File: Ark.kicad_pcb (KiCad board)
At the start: 2 copper layers, 71.9 x 89.1 mm, 109 parts, among them P1 USB_OTG, P2 USB_OTG, P3 40_Pin_LCD_Out, P4 6_Pin_Touch_In, Q1 MMUN2133LT1G, SW1 SW_PUSH_SMALL_H, SW2 SW_PUSH_SMALL_H, SW3 SW_PUSH_SMALL_H, SW4 SW_PUSH_SMALL_H, SW5 SW_PUSH_SMALL_H, SW6 SW_PUSH_SMALL_H, U1 PAM2306AYPKE, U2 AP7115-25SEG, U3 DDR2_SODIMM_CM_3_Lite, U4 1040310811, U5 FAN5333BSX, U6 TPS61090RSAR, U7 MCP73871, U8 SPDT_switch

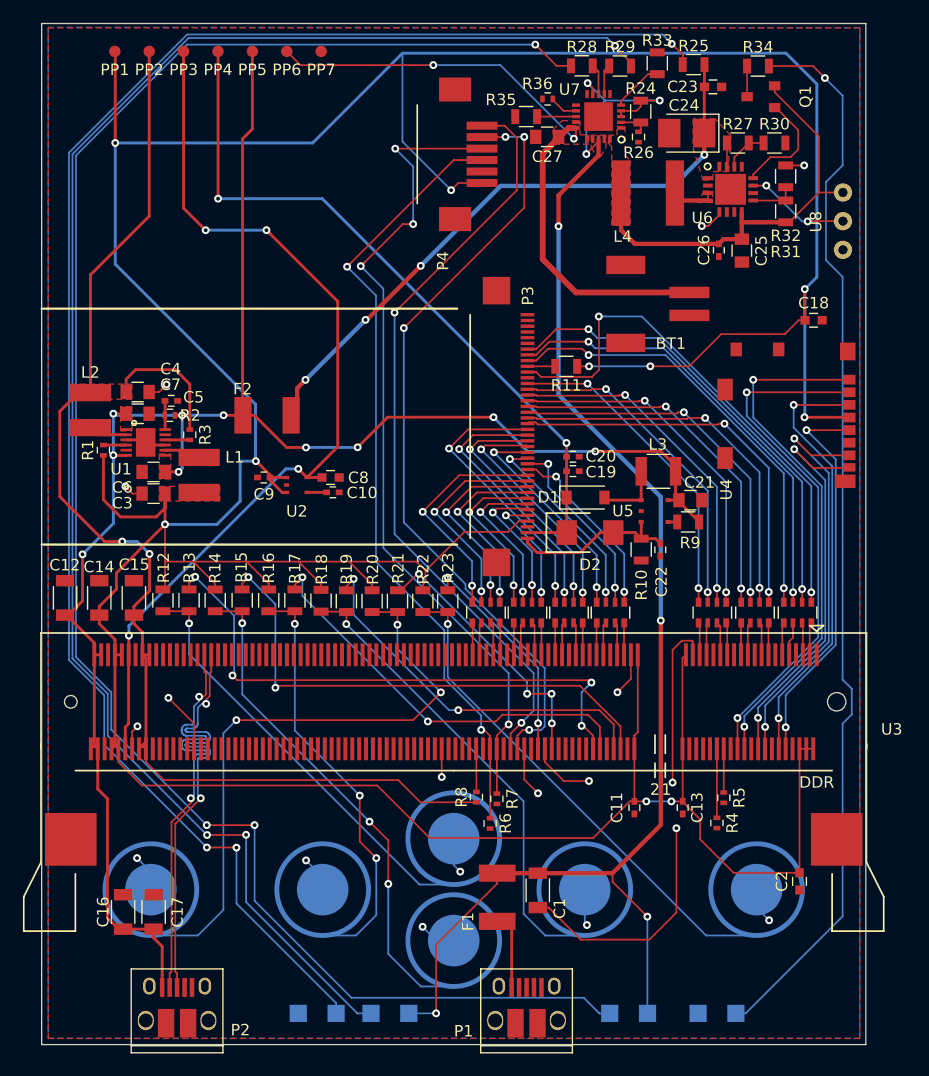
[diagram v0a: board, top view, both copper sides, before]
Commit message: Added grouding vias
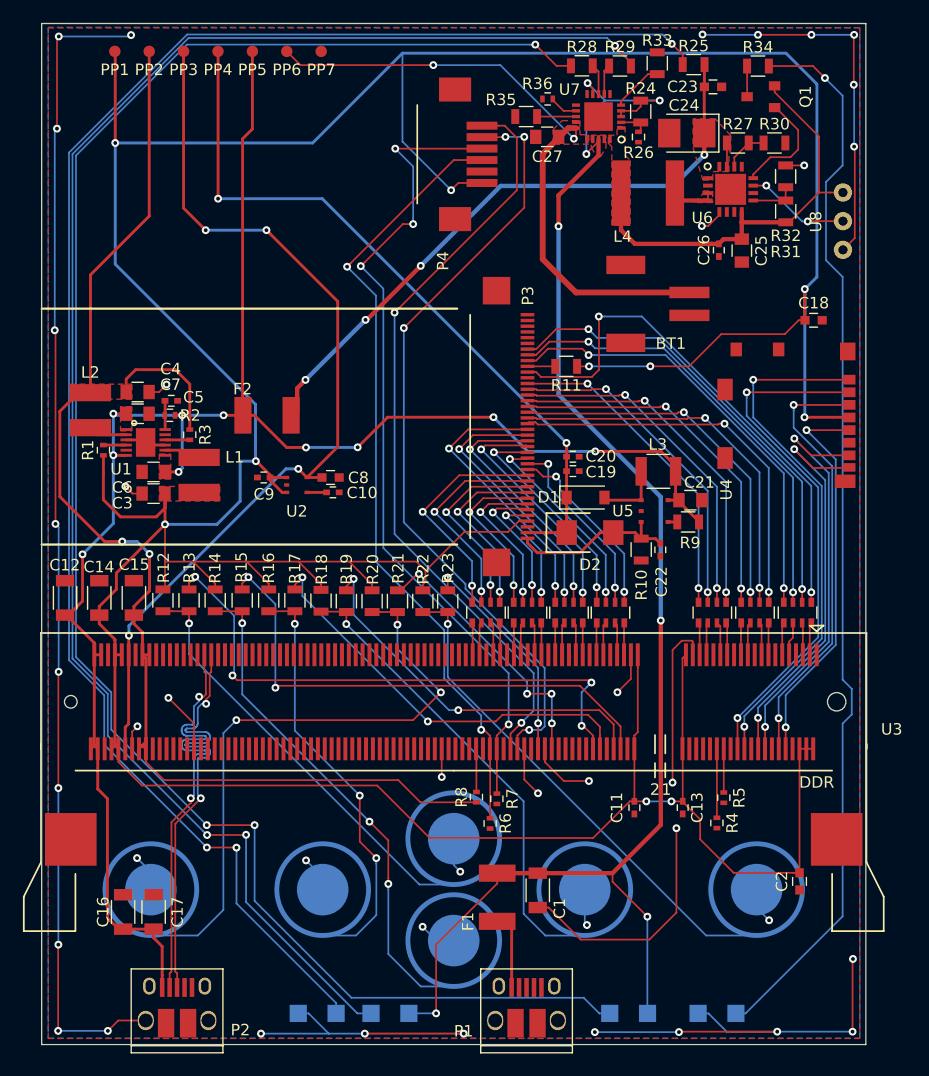
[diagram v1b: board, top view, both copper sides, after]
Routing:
- net GND: track 90.2 -> 290.1 mm, vias 18 -> 42
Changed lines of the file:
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@@
     (thickness 1.6002)
     (drawings 12)
-    (tracks 1414)
+    (tracks 1482)
     (zones 0)
     (modules 109)
@@
   (gr_line (start 103.759 167.0558) (end 175.641 167.0558) (layer Edge.Cuts) (width 0.1))
   (gr_line (start 103.759 78) (end 175.641 78) (layer Edge.Cuts) (width 0.1))
+  (segment (start 105.25252 79.13116) (end 111.43488 79.13116) (width 0.1524) (layer B.Cu) (net 1))
+  (segment (start 111.43488 79.13116) (end 111.5568 79.00924) (width 0.1524) (layer B.Cu) (net 1))
+  (via (at 111.5568 79.00924) (size 0.6858) (drill 0.3302) (layers F.Cu B.Cu) (net 1))
+  (segment (start 105.09504 87.17026) (end 105.09504 79.28864) (width 0.1524) (layer F.Cu) (net 1))
+  (segment (start 105.09504 79.28864) (end 105.25252 79.13116) (width 0.1524) (layer F.Cu) (net 1))
+  (via (at 105.25252 79.13116) (size 0.6858) (drill 0.3302) (layers F.Cu B.Cu) (net 1))
+  (segment (start 104.89946 104.75468) (end 104.89946 87.36584) (width 0.1524) (layer B.Cu) (net 1))
+  (segment (start 104.89946 87.36584) (end 105.09504 87.17026) (width 0.1524) (layer B.Cu) (net 1))
+  (via (at 105.09504 87.17026) (size 0.6858) (drill 0.3302) (layers F.Cu B.Cu) (net 1))
+  (segment (start 104.9655 121.64314) (end 104.9655 104.82072) (width 0.1524) (layer F.Cu) (net 1))
+  (segment (start 104.9655 104.82072) (end 104.89946 104.75468) (width 0.1524) (layer F.Cu) (net 1))
+  (via (at 104.89946 104.75468) (size 0.6858) (drill 0.3302) (layers F.Cu B.Cu) (net 1))
+  (segment (start 105.23982 134.54634) (end 105.23982 121.91746) (width 0.1524) (layer B.Cu) (net 1))
+  (via (at 104.9655 121.64314) (size 0.6858) (drill 0.3302) (layers F.Cu B.Cu) (net 1))
+  (segment (start 105.23982 121.91746) (end 104.9655 121.64314) (width 0.1524) (layer B.Cu) (net 1))
+  (segment (start 105.21696 144.68348) (end 105.21696 134.5692) (width 0.1524) (layer F.Cu) (net 1))
+  (segment (start 105.21696 134.5692) (end 105.23982 134.54634) (width 0.1524) (layer F.Cu) (net 1))
+  (via (at 105.23982 134.54634) (size 0.6858) (drill 0.3302) (layers F.Cu B.Cu) (net 1))
+  (segment (start 105.21696 158.34106) (end 105.21696 144.68348) (width 0.1524) (layer B.Cu) (net 1))
+  (via (at 105.21696 144.68348) (size 0.6858) (drill 0.3302) (layers F.Cu B.Cu) (net 1))
+  (segment (start 105.1941 165.862) (end 105.1941 158.36392) (width 0.1524) (layer F.Cu) (net 1))
+  (segment (start 105.1941 158.36392) (end 105.21696 158.34106) (width 0.1524) (layer F.Cu) (net 1))
+  (via (at 105.21696 158.34106) (size 0.6858) (drill 0.3302) (layers F.Cu B.Cu) (net 1))
+  (segment (start 109.53242 165.862) (end 105.1941 165.862) (width 0.1524) (layer B.Cu) (net 1))
+  (via (at 105.1941 165.862) (size 0.6858) (drill 0.3302) (layers F.Cu B.Cu) (net 1))
+  (segment (start 112.84 164.956) (end 110.43842 164.956) (width 0.1524) (layer F.Cu) (net 1))
+  (segment (start 110.43842 164.956) (end 109.53242 165.862) (width 0.1524) (layer F.Cu) (net 1))
+  (via (at 109.53242 165.862) (size 0.6858) (drill 0.3302) (layers F.Cu B.Cu) (net 1))
+  (segment (start 128.8051 166.10076) (end 122.89028 166.10076) (width 0.1524) (layer B.Cu) (net 1))
+  (via (at 122.89028 166.10076) (size 0.6858) (drill 0.3302) (layers F.Cu B.Cu) (net 1))
+  (segment (start 128.8051 166.10076) (end 131.94284 166.10076) (width 0.1524) (layer B.Cu) (net 1))
+  (segment (start 131.94284 166.10076) (end 140.56868 166.10076) (width 0.1524) (layer B.Cu) (net 1))
+  (segment (start 140.56868 166.10076) (end 131.94284 166.10076) (width 0.1524) (layer F.Cu) (net 1))
+  (via (at 131.94284 166.10076) (size 0.6858) (drill 0.3302) (layers F.Cu B.Cu) (net 1))
+  (segment (start 126.13994 164.338) (end 127.04234 164.338) (width 0.1524) (layer B.Cu) (net 1))
+  (segment (start 127.04234 164.338) (end 128.8051 166.10076) (width 0.1524) (layer B.Cu) (net 1))
+  (via (at 140.56868 166.10076) (size 0.6858) (drill 0.3302) (layers F.Cu B.Cu) (net 1))
+  (segment (start 159.34436 165.96868) (end 152.0063 165.96868) (width 0.1524) (layer B.Cu) (net 1))
+  (via (at 152.0063 165.96868) (size 0.6858) (drill 0.3302) (layers F.Cu B.Cu) (net 1))
+  (segment (start 167.91432 165.93058) (end 159.38246 165.93058) (width 0.1524) (layer F.Cu) (net 1))
+  (segment (start 159.38246 165.93058) (end 159.34436 165.96868) (width 0.1524) (layer F.Cu) (net 1))
+  (via (at 159.34436 165.96868) (size 0.6858) (drill 0.3302) (layers F.Cu B.Cu) (net 1))
+  (segment (start 167.91432 165.93058) (end 174.48276 165.93058) (width 0.1524) (layer B.Cu) (net 1))
+  (segment (start 163.50658 165.93058) (end 167.91432 165.93058) (width 0.1524) (layer B.Cu) (net 1))
+  (via (at 167.91432 165.93058) (size 0.6858) (drill 0.3302) (layers F.Cu B.Cu) (net 1))
+  (segment (start 174.48276 165.93058) (end 174.48276 159.62884) (width 0.1524) (layer F.Cu) (net 1))
+  (segment (start 174.48276 159.62884) (end 174.52086 159.59074) (width 0.1524) (layer F.Cu) (net 1))
+  (via (at 174.52086 159.59074) (size 0.6858) (drill 0.3302) (layers F.Cu B.Cu) (net 1))
+  (segment (start 161.0116 164.338) (end 161.914 164.338) (width 0.1524) (layer B.Cu) (net 1))
+  (segment (start 161.914 164.338) (end 163.50658 165.93058) (width 0.1524) (layer B.Cu) (net 1))
+  (via (at 174.48276 165.93058) (size 0.6858) (drill 0.3302) (layers F.Cu B.Cu) (net 1))
+  (segment (start 166.23284 78.98638) (end 161.42716 78.98638) (width 0.1524) (layer B.Cu) (net 1))
+  (segment (start 161.42716 78.98638) (end 161.39922 78.95844) (width 0.1524) (layer B.Cu) (net 1))
+  (via (at 161.39922 78.95844) (size 0.6858) (drill 0.3302) (layers F.Cu B.Cu) (net 1))
+  (segment (start 170.89628 78.98638) (end 166.23284 78.98638) (width 0.1524) (layer F.Cu) (net 1))
+  (via (at 166.23284 78.98638) (size 0.6858) (drill 0.3302) (layers F.Cu B.Cu) (net 1))
+  (segment (start 174.61992 78.98638) (end 170.89628 78.98638) (width 0.1524) (layer B.Cu) (net 1))
+  (via (at 170.89628 78.98638) (size 0.6858) (drill 0.3302) (layers F.Cu B.Cu) (net 1))
+  (segment (start 174.59198 83.3374) (end 174.59198 79.01432) (width 0.1524) (layer F.Cu) (net 1))
+  (segment (start 174.59198 79.01432) (end 174.61992 78.98638) (width 0.1524) (layer F.Cu) (net 1))
+  (via (at 174.61992 78.98638) (size 0.6858) (drill 0.3302) (layers F.Cu B.Cu) (net 1))
+  (segment (start 174.61992 88.73744) (end 174.61992 83.36534) (width 0.1524) (layer B.Cu) (net 1))
+  (segment (start 174.61992 83.36534) (end 174.59198 83.3374) (width 0.1524) (layer B.Cu) (net 1))
+  (via (at 174.59198 83.3374) (size 0.6858) (drill 0.3302) (layers F.Cu B.Cu) (net 1))
+  (segment (start 173.6471 97.73984) (end 174.675701 96.711239) (width 0.1524) (layer F.Cu) (net 1))
+  (segment (start 174.675701 96.711239) (end 174.675701 88.793221) (width 0.1524) (layer F.Cu) (net 1))
+  (segment (start 174.675701 88.793221) (end 174.61992 88.73744) (width 0.1524) (layer F.Cu) (net 1))
+  (via (at 174.61992 88.73744) (size 0.6858) (drill 0.3302) (layers F.Cu B.Cu) (net 1))
   (segment (start 147.0279 155.10536) (end 147.9803 155.10536) (width 0.1524) (layer F.Cu) (net 1))
   (segment (start 147.9803 155.10536) (end 150.77658 157.90164) (width 0.1524) (layer F.Cu) (net 1))

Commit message: Added mounting holes and cal points
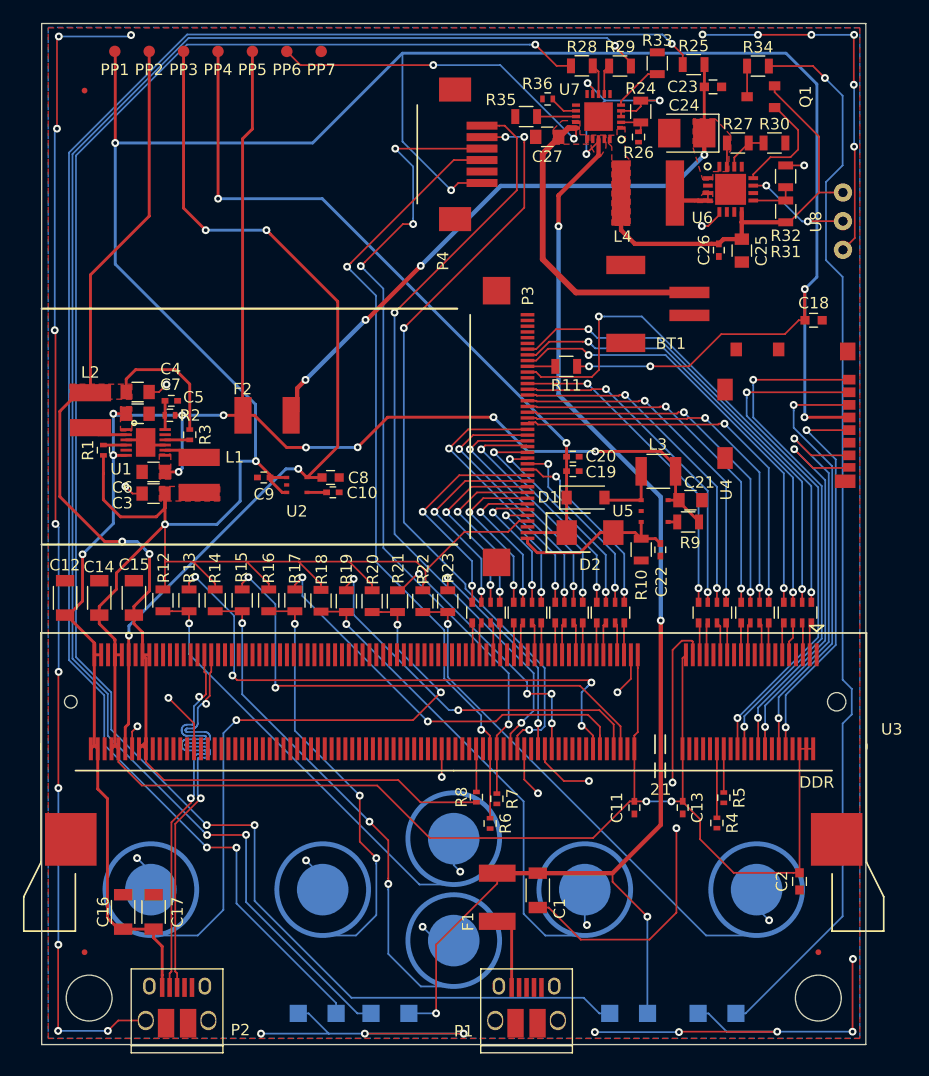
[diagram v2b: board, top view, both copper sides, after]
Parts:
- added P5: CONN_01X01, Pi-Library:Fiducial, F.Cu at (107.5, 83.8)
- added P6: CONN_01X01, Pi-Library:Fiducial, F.Cu at (107.5, 159.0)
- added P7: CONN_01X01, Pi-Library:Fiducial, F.Cu at (171.5, 159.0)
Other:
- outline, holes or cut-outs redrawn
- board text added: "Low Batt"
- board text added: "v1.0"
- board text removed: "Low Battery"
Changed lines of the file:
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@@
     (links 372)
     (no_connects 0)
-    (area 101.972599 77.9044 179.0524 170.7734)
+    (area 103.708999 77.949999 175.691001 167.105801)
     (thickness 1.6002)
-    (drawings 12)
+    (drawings 15)
     (tracks 1482)
     (zones 0)
-    (modules 109)
-    (nets 205)
+    (modules 112)
+    (nets 208)
   )
   (page USLetter)
@@
     (mod_text_size 1 1)
     (mod_text_width 0.15)
-    (pad_size 1.5 1.5)
-    (pad_drill 0.6)
+    (pad_size 1 1)
+    (pad_drill 0)
     (pad_to_mask_clearance 0)
     (aux_axis_origin 0 0)
@@
   (net 203 "Net-(U3-Pad64)")
   (net 204 "Net-(U3-Pad72)")
+  (net 205 "Net-(P5-Pad1)")
+  (net 206 "Net-(P6-Pad1)")
+  (net 207 "Net-(P7-Pad1)")
   (net_class Default "This is the default net class."
     (clearance 0.1524)
@@
     (add_net "Net-(P3-Pad8)")
     (add_net "Net-(P3-Pad9)")
+    (add_net "Net-(P5-Pad1)")
+    (add_net "Net-(P6-Pad1)")
+    (add_net "Net-(P7-Pad1)")
     (add_net "Net-(Q1-Pad1)")
     (add_net "Net-(Q1-Pad3)")
@@
       (effects (font (size 1 1) (thickness 0.15)))
     )
-    (pad 1 smd circle (at 0 0) (size 1 1) (layers F.Cu F.Paste F.Mask)
+    (pad 1 smd circle (at 0 0) (size 1 1) (layers F.Cu F.Mask)
       (net 1 GND))
   )
@@
       (effects (font (size 1 1) (thickness 0.15)))
     )
-    (pad 1 smd circle (at 0 0) (size 1 1) (layers F.Cu F.Paste F.Mask)
+    (pad 1 smd circle (at 0 0) (size 1 1) (layers F.Cu F.Mask)
       (net 2 "Net-(BT1-Pad1)"))
   )
@@
       (effects (font (size 1 1) (thickness 0.15)))
     )
-    (pad 1 smd circle (at 0 0) (size 1 1) (layers F.Cu F.Paste F.Mask)
+    (pad 1 smd circle (at 0 0) (size 1 1) (layers F.Cu F.Mask)
       (net 7 5V))
   )
@@
       (effects (font (size 1 1) (thickness 0.15)))
     )
-    (pad 1 smd circle (at 0 0) (size 1 1) (layers F.Cu F.Paste F.Mask)
+    (pad 1 smd circle (at 0 0) (size 1 1) (layers F.Cu F.Mask)
       (net 10 24V))
   )
@@
       (effects (font (size 1 1) (thickness 0.15)))
     )
-    (pad 1 smd circle (at 0 0) (size 1 1) (layers F.Cu F.Paste F.Mask)
+    (pad 1 smd circle (at 0 0) (size 1 1) (layers F.Cu F.Mask)
       (net 8 CM_VDAC))
   )
@@
       (effects (font (size 1 1) (thickness 0.15)))
     )
-    (pad 1 smd circle (at 0 0) (size 1 1) (layers F.Cu F.Paste F.Mask)
+    (pad 1 smd circle (at 0 0) (size 1 1) (layers F.Cu F.Mask)
       (net 5 1V8))
   )
@@
       (effects (font (size 1 1) (thickness 0.15)))
     )
-    (pad 1 smd circle (at 0 0) (size 1 1) (layers F.Cu F.Paste F.Mask)
+    (pad 1 smd circle (at 0 0) (size 1 1) (layers F.Cu F.Mask)
       (net 4 3V3))
   )
@@
   (module Pi-Library:Snapdome_SW (layer B.Cu)
     (at 139.7 157.988)
-    (fp_text reference SW6 (at -6.02742 0.23368) (layer B.SilkS)
+    (fp_text reference SW6 (at -6.10362 -0.05588) (layer B.SilkS)
       (effects (font (size 1 1) (thickness 0.15)) (justify mirror))
     )
@@
   (module Pi-Library:Snapdome_SW (layer B.Cu)
     (at 166.116 153.543)
-    (fp_text reference SW5 (at -4.45008 3.78714) (layer B.SilkS)
+    (fp_text reference SW5 (at -0.00254 -5.12826) (layer B.SilkS)
       (effects (font (size 1 1) (thickness 0.15)) (justify mirror))
     )
@@
   (module Pi-Library:Snapdome_SW (layer B.Cu)
     (at 151.13 153.543)
-    (fp_text reference SW4 (at 4.73202 3.65506) (layer B.SilkS)
+    (fp_text reference SW4 (at 0.01016 -5.17398) (layer B.SilkS)
       (effects (font (size 1 1) (thickness 0.15)) (justify mirror))
     )
@@
   (module Pi-Library:Snapdome_SW (layer B.Cu)
     (at 128.27 153.543)
-    (fp_text reference SW3 (at -5.14858 -2.90576) (layer B.SilkS)
+    (fp_text reference SW3 (at 0.04826 -5.26288) (layer B.SilkS)
       (effects (font (size 1 1) (thickness 0.15)) (justify mirror))
     )
@@
   (module Pi-Library:Snapdome_SW (layer B.Cu)
     (at 139.7 149.098)
-    (fp_text reference SW1 (at -3.91668 -3.93446) (layer B.SilkS)
+    (fp_text reference SW1 (at -6.01472 0.08382) (layer B.SilkS)
       (effects (font (size 1 1) (thickness 0.15)) (justify mirror))
     )
@@
     (pad "" smd rect (at -5.65 2.35 270) (size 2.1 2.8) (layers F.Cu F.Paste F.Mask))
   )
+  (module Pi-Library:Fiducial (layer F.Cu)
+    (at 107.5 83.85)
+    (fp_text reference P5 (at 0 2.1) (layer F.SilkS) hide
+      (effects (font (size 1 1) (thickness 0.15)))
+    )
+    (fp_text value CONN_01X01 (at 0 -2) (layer F.Fab)
+      (effects (font (size 1 1) (thickness 0.15)))
+    )
+    (pad 1 smd circle (at 0 0) (size 0.5 0.5) (layers F.Cu F.Mask)
+      (net 205 "Net-(P5-Pad1)") (solder_mask_margin 1))
+  )
+  (module Pi-Library:Fiducial (layer F.Cu)
+    (at 107.5 159)
+    (fp_text reference P6 (at 0 2.1) (layer F.SilkS) hide
+      (effects (font (size 1 1) (thickness 0.15)))
+    )
+    (fp_text value CONN_01X01 (at 0 -2) (layer F.Fab)
+      (effects (font (size 1 1) (thickness 0.15)))
+    )
+    (pad 1 smd circle (at 0 0) (size 0.5 0.5) (layers F.Cu F.Mask)
+      (net 206 "Net-(P6-Pad1)") (solder_mask_margin 1))
+  )
+  (module Pi-Library:Fiducial (layer F.Cu)
+    (at 171.5 159)
+    (fp_text reference P7 (at 0 2.1) (layer F.SilkS) hide
+      (effects (font (size 1 1) (thickness 0.15)))
+    )
+    (fp_text value CONN_01X01 (at 0 -2) (layer F.Fab)
+      (effects (font (size 1 1) (thickness 0.15)))
+    )
+    (pad 1 smd circle (at 0 0) (size 0.5 0.5) (layers F.Cu F.Mask)
+      (net 207 "Net-(P7-Pad1)") (solder_mask_margin 1))
+  )
+  (gr_circle (center 107.9 163) (end 109.9 163) (layer Edge.Cuts) (width 0.1))
+  (gr_circle (center 171.5 163) (end 173.5 163) (layer Edge.Cuts) (width 0.1))
+  (gr_text v1.0 (at 119.74068 124.55906) (layer B.SilkS)
+    (effects (font (size 3.5 3.5) (thickness 0.3)) (justify mirror))
+  )
   (gr_text "The Ark" (at 139.7 114.3) (layer B.SilkS)
     (effects (font (size 12.7 12.7) (thickness 0.762) italic) (justify mirror))
   )
-  (gr_text On (at 127.78232 161.85388) (layer B.SilkS)
+  (gr_text On (at 127.82296 159.42056) (layer B.SilkS)
     (effects (font (size 1.5 1.5) (thickness 0.3)) (justify mirror))
   )
-  (gr_text Charging (at 154.97302 161.95802) (layer B.SilkS)
+  (gr_text Charging (at 155.9687 161.90214) (layer B.SilkS)
     (effects (font (size 1.5 1.5) (thickness 0.3)) (justify mirror))
   )
-  (gr_text Charged (at 135.41502 161.8742) (layer B.SilkS)
+  (gr_text Charged (at 132.10794 162.03676) (layer B.SilkS)
     (effects (font (size 1.5 1.5) (thickness 0.3)) (justify mirror))
   )
-  (gr_text "Low Battery" (at 167.6527 161.85388) (layer B.SilkS)
+  (gr_text "Low Batt" (at 162.68954 159.46628) (layer B.SilkS)
     (effects (font (size 1.5 1.5) (thickness 0.3)) (justify mirror))
   )
@@
       )
     )
+  )
+  (zone (net 0) (net_name "") (layer F.Cu) (hatch edge 0.508)
+    (connect_pads (clearance 0.1524))
+    (min_thickness 0.254)
+    (keepout (tracks allowed) (vias allowed) (copperpour not_allowed))
+    (fill (arc_segments 16) (thermal_gap 0.508) (thermal_bridge_width 0.508))
+    (polygon
+      (pts
+        (xy 106.09834 157.64002) (xy 106.09834 160.3883) (xy 109.0422 160.3883) (xy 109.0422 157.59176) (xy 109.03966 157.58922)
+      )
+    )
+  )
+  (zone (net 0) (net_name "") (layer F.Cu) (hatch edge 0.508)
+    (connect_pads (clearance 0.1524))
+    (min_thickness 0.254)
+    (keepout (tracks allowed) (vias allowed) (copperpour not_allowed))
+    (fill (arc_segments 16) (thermal_gap 0.508) (thermal_bridge_width 0.508))
+    (polygon
+      (pts
+        (xy 170.0276 157.63748) (xy 170.0276 160.3248) (xy 173.07814 160.3248) (xy 173.07814 157.56636) (xy 173.0502 157.53842)
+      )
+    )
+  )
+  (zone (net 0) (net_name "") (layer F.Cu) (hatch edge 0.508)
+    (connect_pads (clearance 0.1524))
+    (min_thickness 0.254)
+    (keepout (tracks allowed) (vias allowed) (copperpour not_allowed))
+    (fill (arc_segments 16) (thermal_gap 0.508) (thermal_bridge_width 0.508))
+    (polygon
+      (pts
+        (xy 106.07548 82.45602) (xy 106.07548 85.27034) (xy 108.91266 85.27034) (xy 108.91266 82.43062) (xy 108.8771 82.39506)
+      )
+    )
